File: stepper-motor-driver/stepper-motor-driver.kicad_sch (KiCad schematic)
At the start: 0 parts

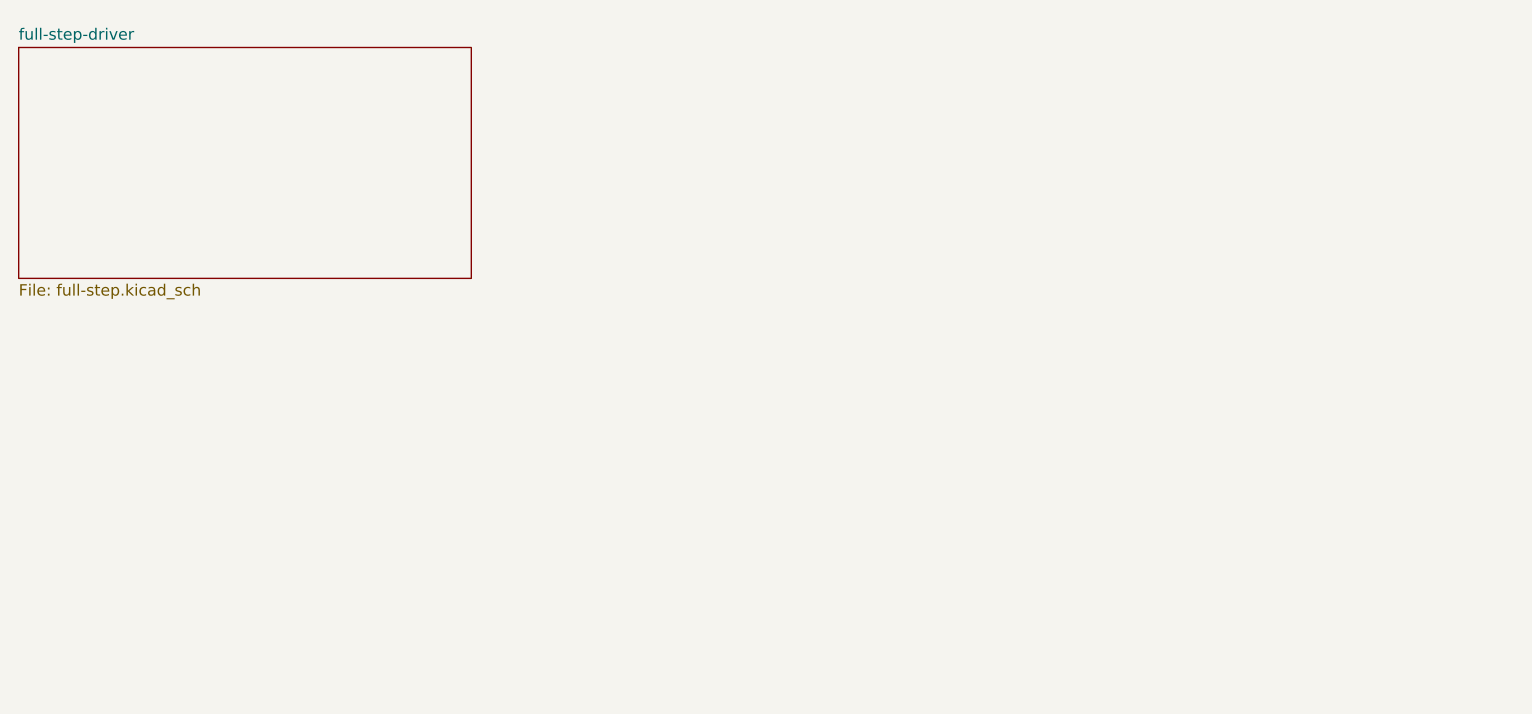
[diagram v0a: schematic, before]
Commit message: schematic mostly done except gate drivers
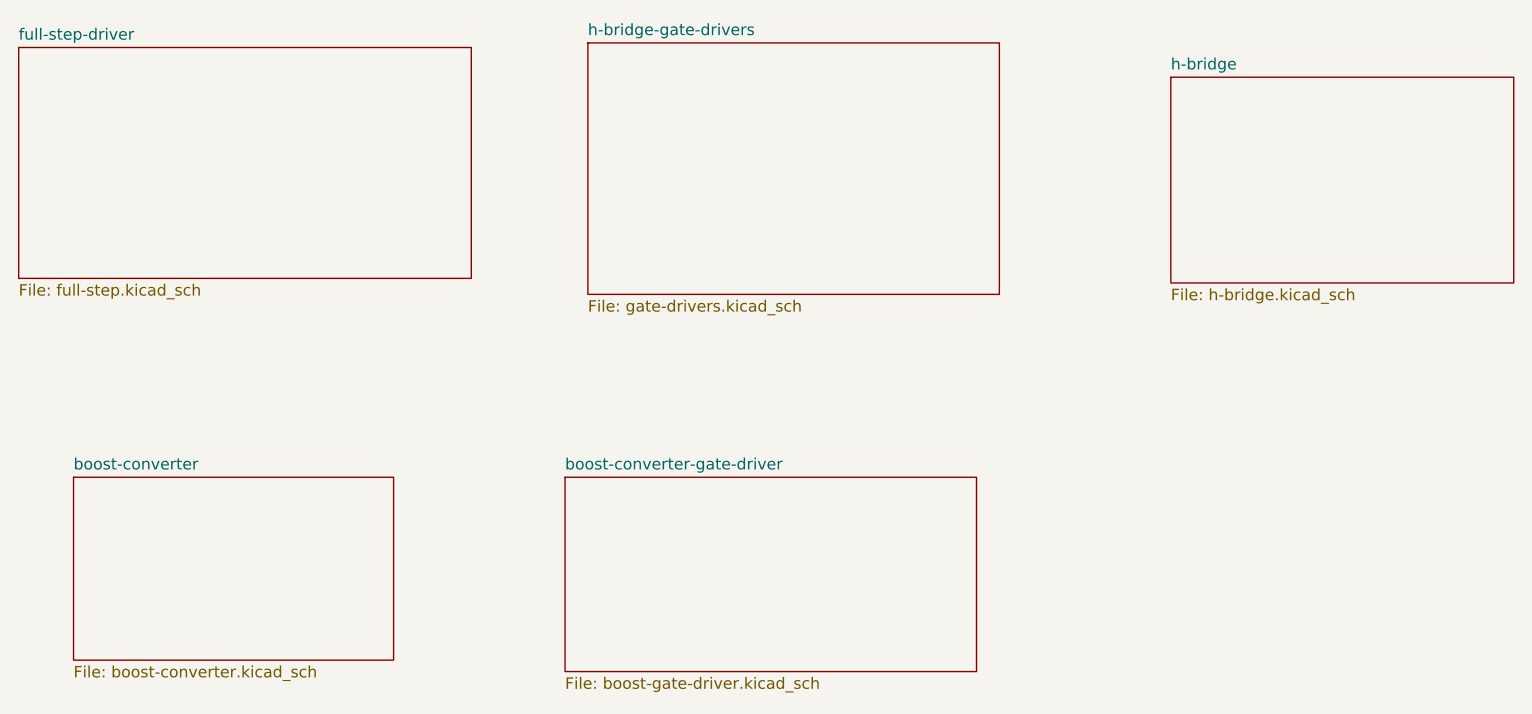
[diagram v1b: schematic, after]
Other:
- added sheet boost-converter (boost-converter.kicad_sch)
- added sheet boost-converter-gate-driver (boost-gate-driver.kicad_sch)
- added sheet h-bridge (h-bridge.kicad_sch)
- added sheet h-bridge-gate-drivers (gate-drivers.kicad_sch)
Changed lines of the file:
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@@
 	(paper "A4")
+	(sheet
+		(at 153.67 29.21)
+		(size 38.1 22.86)
+		(exclude_from_sim no)
+		(in_bom yes)
+		(on_board yes)
+		(dnp no)
+		(fields_autoplaced yes)
+		(stroke
+			(width 0.1524)
+			(type solid)
+		)
+		(fill
+			(color 0 0 0 0.0000)
+		)
+		(property "Sheetname" "h-bridge"
+			(at 153.67 28.4984 0)
+			(effects
+				(font
+					(size 1.27 1.27)
+				)
+				(justify left bottom)
+			)
+		)
+		(property "Sheetfile" "h-bridge.kicad_sch"
+			(at 153.67 52.6546 0)
+			(effects
+				(font
+					(size 1.27 1.27)
+				)
+				(justify left top)
+			)
+		)
+		(instances
+			(project "stepper-motor-driver"
+				(path "/daa09f9b-cd8d-41e7-aeb1-7c84d26fe45e"
+					(page "3")
+				)
+			)
+		)
+	)
+	(sheet
+		(at 86.36 73.66)
+		(size 45.72 21.59)
+		(exclude_from_sim no)
+		(in_bom yes)
+		(on_board yes)
+		(dnp no)
+		(fields_autoplaced yes)
+		(stroke
+			(width 0.1524)
+			(type solid)
+		)
+		(fill
+			(color 0 0 0 0.0000)
+		)
+		(property "Sheetname" "boost-converter-gate-driver"
+			(at 86.36 72.9484 0)
+			(effects
+				(font
+					(size 1.27 1.27)
+				)
+				(justify left bottom)
+			)
+		)
+		(property "Sheetfile" "boost-gate-driver.kicad_sch"
+			(at 86.36 95.8346 0)
+			(effects
+				(font
+					(size 1.27 1.27)
+				)
+				(justify left top)
+			)
+		)
+		(instances
+			(project "stepper-motor-driver"
+				(path "/daa09f9b-cd8d-41e7-aeb1-7c84d26fe45e"
+					(page "6")
+				)
+			)
+		)
+	)
+	(sheet
+		(at 31.75 73.66)
+		(size 35.56 20.32)
+		(exclude_from_sim no)
+		(in_bom yes)
+		(on_board yes)
+		(dnp no)
+		(fields_autoplaced yes)
+		(stroke
+			(width 0.1524)
+			(type solid)
+		)
+		(fill
+			(color 0 0 0 0.0000)
+		)
+		(property "Sheetname" "boost-converter"
+			(at 31.75 72.9484 0)
+			(effects
+				(font
+					(size 1.27 1.27)
+				)
+				(justify left bottom)
+			)
+		)
+		(property "Sheetfile" "boost-converter.kicad_sch"
+			(at 31.75 94.5646 0)
+			(effects
+				(font
+					(size 1.27 1.27)
+				)
+				(justify left top)
+			)
+		)
+		(instances
+			(project "stepper-motor-driver"
+				(path "/daa09f9b-cd8d-41e7-aeb1-7c84d26fe45e"
+					(page "5")
+				)
+			)
+		)
+	)
+	(sheet
+		(at 88.9 25.4)
+		(size 45.72 27.94)
+		(exclude_from_sim no)
+		(in_bom yes)
+		(on_board yes)
+		(dnp no)
+		(fields_autoplaced yes)
+		(stroke
+			(width 0.1524)
+			(type solid)
+		)
+		(fill
+			(color 0 0 0 0.0000)
+		)
+		(property "Sheetname" "h-bridge-gate-drivers"
+			(at 88.9 24.6884 0)
+			(effects
+				(font
+					(size 1.27 1.27)
+				)
+				(justify left bottom)
+			)
+		)
+		(property "Sheetfile" "gate-drivers.kicad_sch"
+			(at 88.9 53.9246 0)
+			(effects
+				(font
+					(size 1.27 1.27)
+				)
+				(justify left top)
+			)
+		)
+		(instances
+			(project "stepper-motor-driver"
+				(path "/daa09f9b-cd8d-41e7-aeb1-7c84d26fe45e"
+					(page "4")
+				)
+			)
+		)
+	)
 	(sheet
 		(at 25.654 25.908)
